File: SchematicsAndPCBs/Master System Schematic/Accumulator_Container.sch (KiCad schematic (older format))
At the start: 23 parts, among them J1 Shutdown/Precharge Connector, J2 TSAL Connector, J3 Main TS Connector, J4 IMD/TSMP Connector, K1 SPST-NO (Precharge), K2 SPST-NO (AIR), K3 SPST-NO (AIR), K4 SPST-NC (Discharge), K5 SPDT (Precharge Control), SW1 HVD, SW2 SMD, SW3 SMD, U1 TSAL_ISOLATION

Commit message: Updating Library References
Shifting references in the Master Schematic project to use the new NER library
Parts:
- U1: symbol TSV-rescue:TSAL_ISOLATION-FSAE-TSV-shematic-rescue -> NER:TSAL_ISOLATION
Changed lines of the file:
@@
 EESchema Schematic File Version 4
+LIBS:Master System Schematic-cache
 EELAYER 30 0
 EELAYER END
@@
 $EndDescr
 $Comp
-L TSV-rescue:TSAL_ISOLATION-FSAE-TSV-shematic-rescue U1
+L NER:TSAL_ISOLATION U1
 U 1 1 5E5145FA
 P 9900 5450
+AR Path="/5E5145FA" Ref="U1"  Part="1"
+AR Path="/5F45B05E/5E5145FA" Ref="U1"  Part="1"
 F 0 "U1" H 9925 5565 50  0000 C CNN
 F 1 "TSAL_ISOLATION" H 9900 5500 50  0000 C CNN

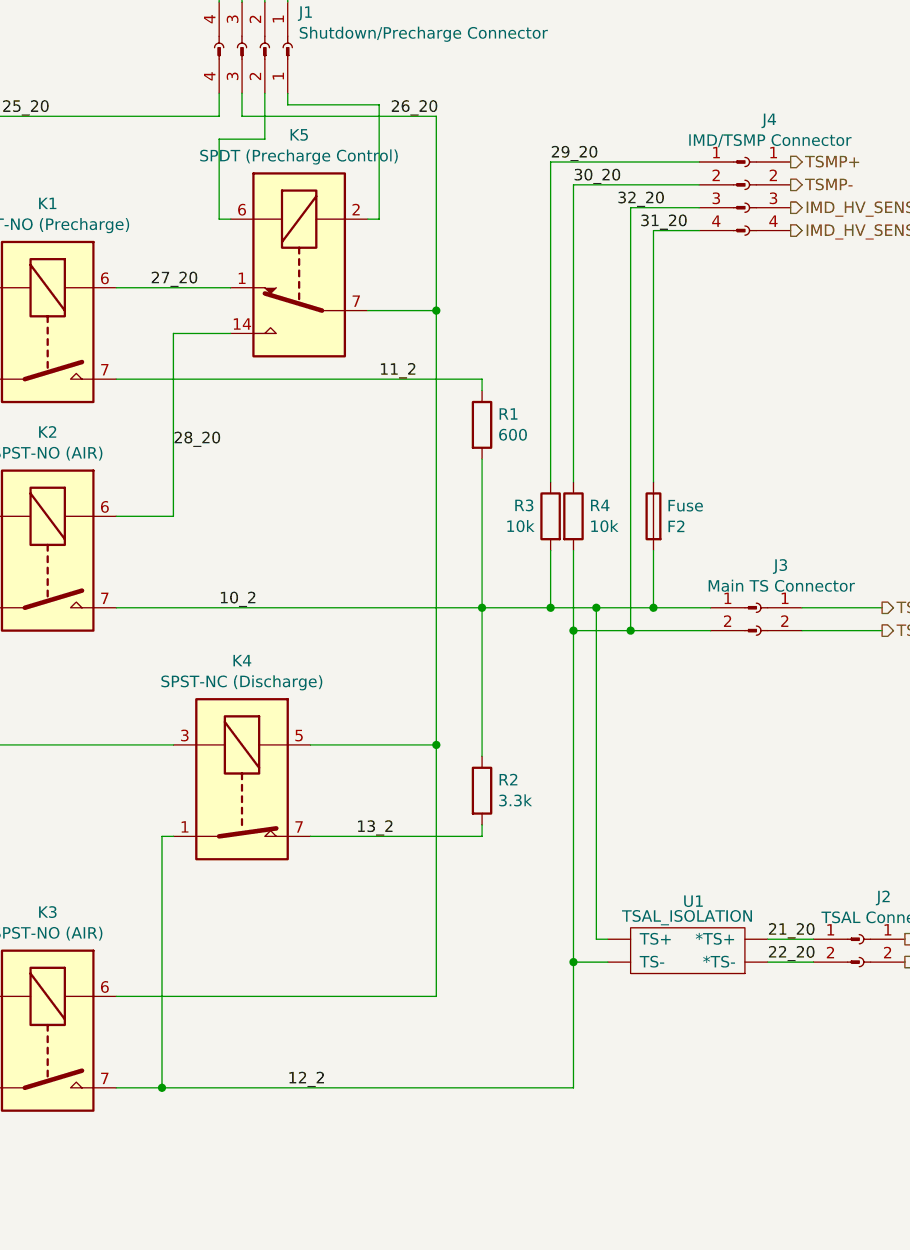
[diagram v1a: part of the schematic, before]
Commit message: Added new IMD fuse
Needed both sense lines to be fused. Added F3 to represent this
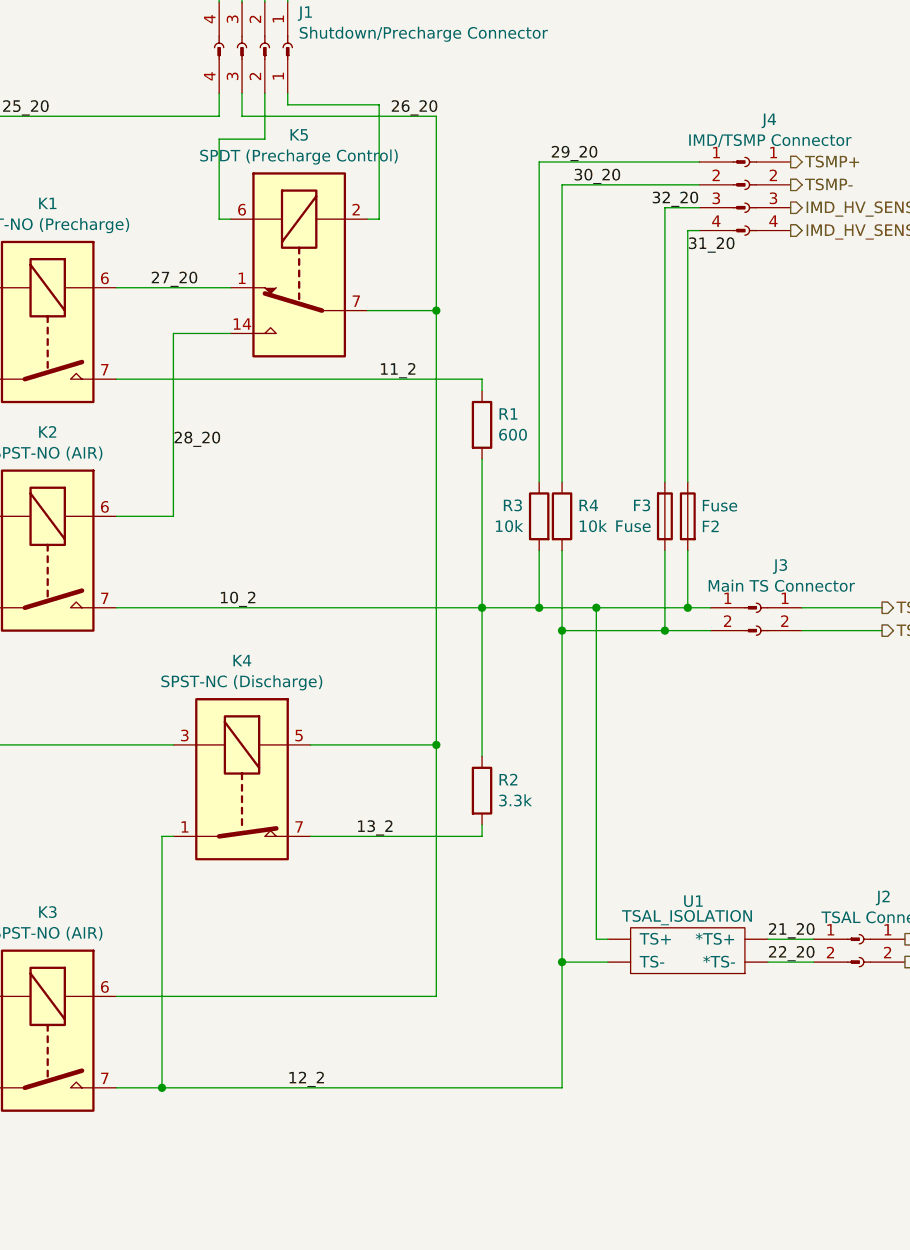
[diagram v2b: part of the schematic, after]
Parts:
- added F3: Fuse, symbol Device:Fuse
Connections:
- net 12_2: now also F3.1; no longer J?.3 (Pin_3)
- new net 32_20: F3.2, J?.3 (Pin_3)
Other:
- moved on the sheet: F2, R3, R4
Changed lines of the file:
@@
 L Device:R R3
 U 1 1 5F2AF3BD
-P 9300 3650
-F 0 "R3" H 9370 3696 50  0000 L CNN
-F 1 "10k" H 9370 3605 50  0000 L CNN
-F 2 "" V 9230 3650 50  0001 C CNN
-F 3 "~" H 9300 3650 50  0001 C CNN
-	1    9300 3650
+P 9250 3650
+F 0 "R3" H 9320 3696 50  0000 L CNN
+F 1 "10k" H 9320 3605 50  0000 L CNN
+F 2 "" V 9180 3650 50  0001 C CNN
+F 3 "~" H 9250 3650 50  0001 C CNN
+	1    9250 3650
 	-1   0    0    -1
 $EndComp
@@
 L Device:R R4
 U 1 1 5F39A796
-P 9400 3650
-F 0 "R4" H 9470 3696 50  0000 L CNN
-F 1 "10k" H 9470 3605 50  0000 L CNN
-F 2 "" V 9330 3650 50  0001 C CNN
-F 3 "~" H 9400 3650 50  0001 C CNN
-	1    9400 3650
+P 9350 3650
+F 0 "R4" H 9420 3696 50  0000 L CNN
+F 1 "10k" H 9420 3605 50  0000 L CNN
+F 2 "" V 9280 3650 50  0001 C CNN
+F 3 "~" H 9350 3650 50  0001 C CNN
+	1    9350 3650
 	1    0    0    -1
 $EndComp
@@
 L Device:Fuse F2
 U 1 1 5F14BDC4
-P 9750 3650
-F 0 "F2" H 9691 3604 50  0000 R CNN
-F 1 "Fuse" H 9691 3695 50  0000 R CNN
-F 2 "" V 9680 3650 50  0001 C CNN
-F 3 "~" H 9750 3650 50  0001 C CNN
-	1    9750 3650
+P 9900 3650
+F 0 "F2" H 9841 3604 50  0000 R CNN
+F 1 "Fuse" H 9841 3695 50  0000 R CNN
+F 2 "" V 9830 3650 50  0001 C CNN
+F 3 "~" H 9900 3650 50  0001 C CNN
+	1    9900 3650
 	-1   0    0    -1
 $EndComp
 Wire Wire Line
-	9750 3800 9750 4050
+	9900 3800 9900 4050
 Text Label 9300 2100 0    50   ~ 0
 29_20
 Text Label 9400 2200 0    50   ~ 0
 30_20
-Text Label 9900 2400 2    50   ~ 0
+Text Label 9900 2500 0    50   ~ 0
 31_20
-Text Label 9800 2300 2    50   ~ 0
+Text Label 9950 2300 2    50   ~ 0
 32_20
 Text Notes 7350 7500 0    50   ~ 0
@@
 $EndComp
 Wire Wire Line
-	9300 2100 9300 3500
-Wire Wire Line
-	9400 2200 9400 3500
-Wire Wire Line
-	9650 2300 9650 4150
-Wire Wire Line
-	9750 2400 9750 3500
-Wire Wire Line
-	9300 2100 9950 2100
-Wire Wire Line
-	9400 2200 9950 2200
-Wire Wire Line
-	9650 2300 9950 2300
-Wire Wire Line
-	9750 2400 9950 2400
-Connection ~ 9300 4050
-Wire Wire Line
-	9300 4050 9300 3800
-Wire Wire Line
-	9000 4050 9300 4050
-Wire Wire Line
-	9300 4050 9500 4050
-Wire Wire Line
-	9400 4150 9650 4150
-Wire Wire Line
-	9400 3800 9400 4150
-Connection ~ 9400 4150
-Connection ~ 9400 5600
-Wire Wire Line
-	9400 4150 9400 5600
+	9250 2100 9250 3500
+Wire Wire Line
+	9350 2200 9350 3500
+Wire Wire Line
+	9800 2300 9800 3500
+Wire Wire Line
+	9900 2400 9900 3500
+Wire Wire Line
+	9800 2300 9950 2300
+Wire Wire Line
+	9900 2400 9950 2400
+Wire Wire Line
+	9250 4050 9250 3800
+Wire Wire Line
+	9000 4050 9250 4050
 Wire Wire Line
 	10250 5500 10450 5500
@@
 Connection ~ 9500 4050
 Wire Wire Line
-	9500 4050 9750 4050
-Wire Wire Line
-	9400 5600 9550 5600
-Wire Wire Line
-	9400 5600 9400 6150
-Wire Wire Line
-	7600 6150 9400 6150
-Connection ~ 9750 4050
-Connection ~ 9650 4150
+	7600 6150 9350 6150
 Wire Wire Line
 	10750 4050 10400 4050
 Wire Wire Line
 	10400 4150 10750 4150
-Wire Wire Line
-	9750 4050 10000 4050
-Wire Wire Line
-	9650 4150 10000 4150
 $Sheet
 S 3200 4800 1550 2350
@@
 Wire Bus Line
 	550  7750 5500 7750
+$Comp
+L Device:Fuse F3
+U 1 1 5F6433FB
+P 9800 3650
+F 0 "F3" H 9741 3604 50  0000 R CNN
+F 1 "Fuse" H 9741 3695 50  0000 R CNN
+F 2 "" V 9730 3650 50  0001 C CNN
+F 3 "~" H 9800 3650 50  0001 C CNN
+	1    9800 3650
+	1    0    0    1
+$EndComp
+Wire Wire Line
+	9800 3800 9800 4150
+Connection ~ 9800 4150
+Wire Wire Line
+	9800 4150 10000 4150
+Connection ~ 9900 4050
+Wire Wire Line
+	9900 4050 10000 4050
+Wire Wire Line
+	9500 4050 9900 4050
+Connection ~ 9250 4050
+Wire Wire Line
+	9250 4050 9500 4050
+Wire Wire Line
+	9350 2200 9950 2200
+Wire Wire Line
+	9250 2100 9950 2100
+Wire Wire Line
+	9350 3800 9350 4150
+Wire Wire Line
+	9350 5600 9550 5600
+Connection ~ 9350 5600
+Wire Wire Line
+	9350 5600 9350 6150
+Wire Wire Line
+	9350 4150 9800 4150
 Wire Bus Line
 	3100 1100 3100 1350
@@
 Wire Bus Line
 	3100 4950 3100 6050
+Connection ~ 9350 4150
+Wire Wire Line
+	9350 4150 9350 5600
 $EndSCHEMATC

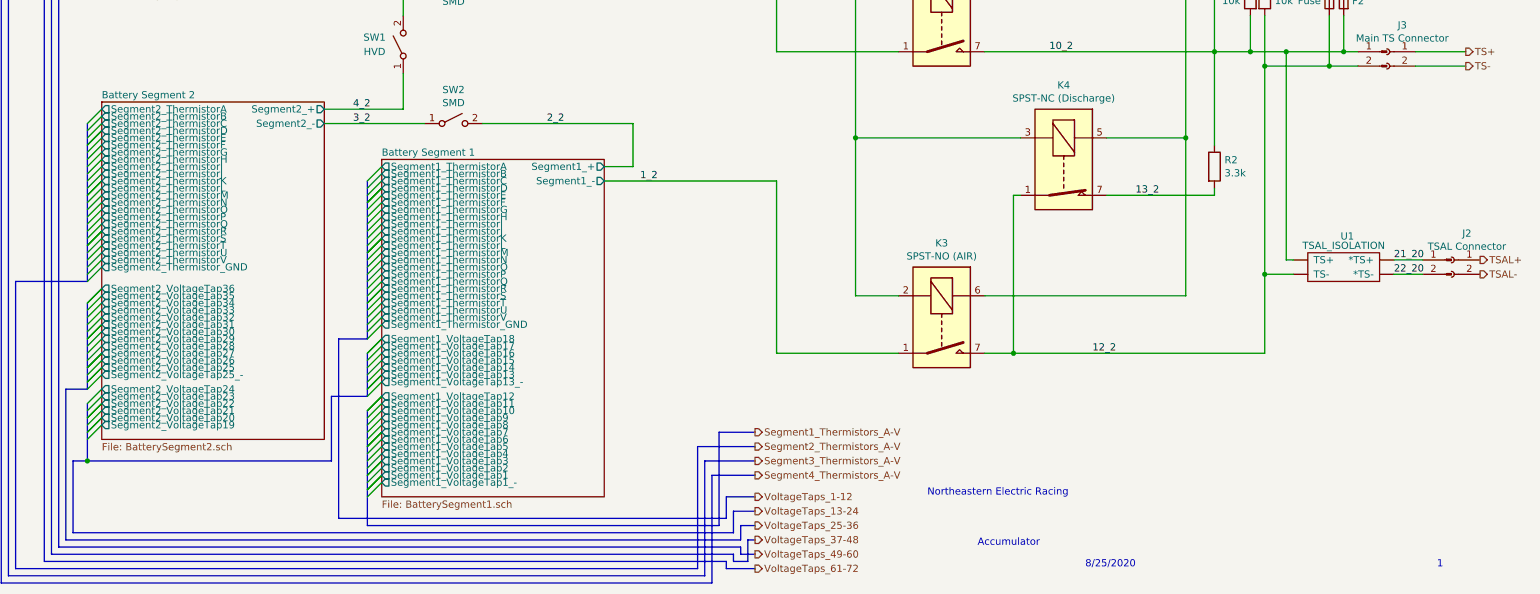
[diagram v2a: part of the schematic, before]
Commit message: Paper Size and Title Blocks
-Switched all paper sizes over to America units  (letter size A and tabloid size B) (so we can actually be cool and print them an stuff)
-Fixed title blocks to use sheet properties
-Started some changes to the accumulator segment schematic
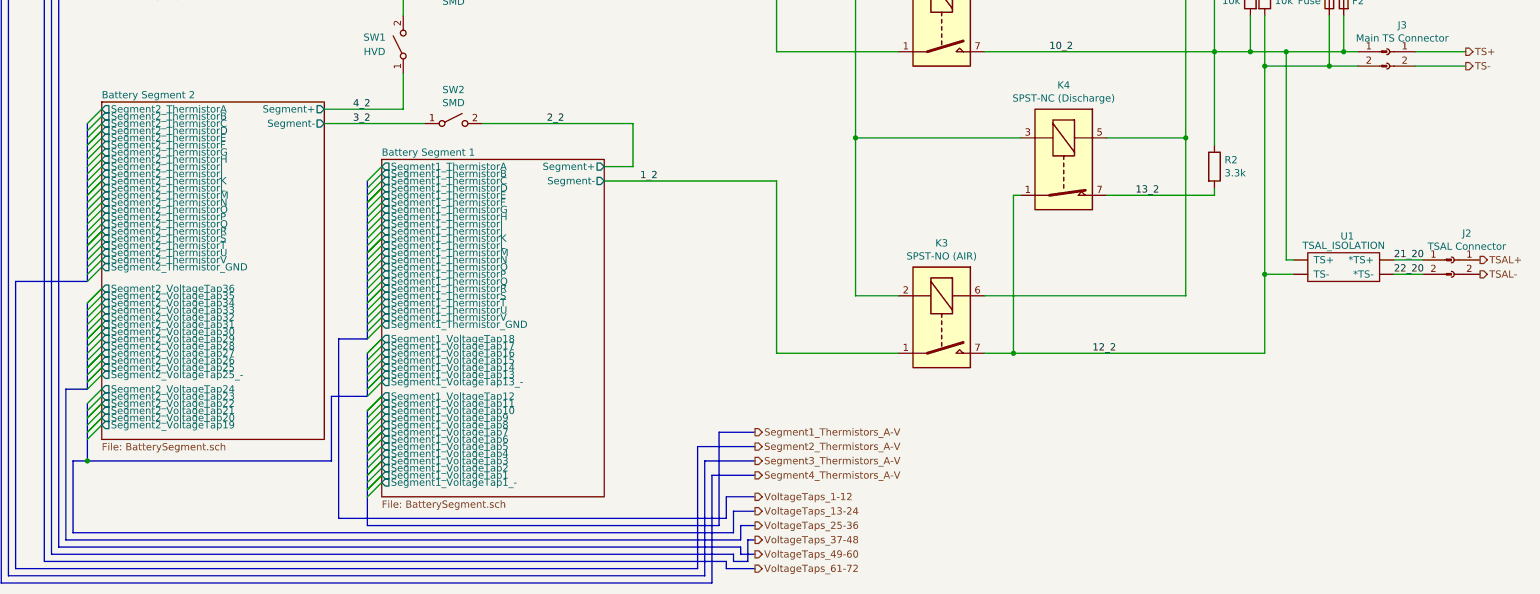
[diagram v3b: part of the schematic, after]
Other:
- note removed: "1"
- note removed: "8/25/2020"
- note removed: "Accumulator"
- note removed: "Northeastern Electric Racing"

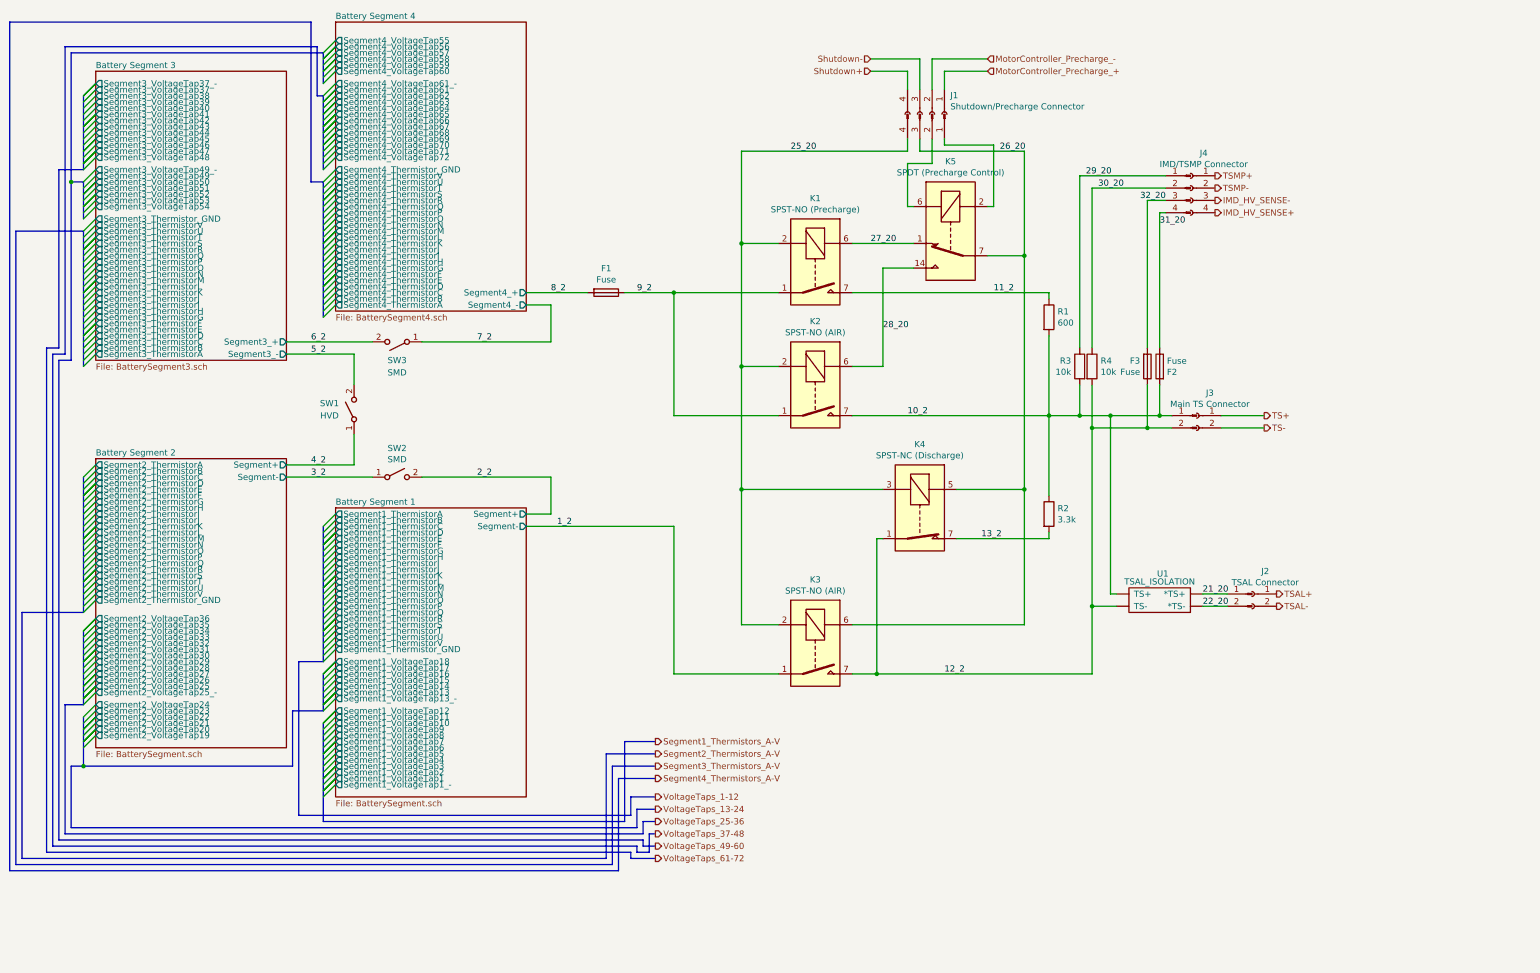
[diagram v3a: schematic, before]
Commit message: Therms and Volt Taps
Mostly fixed all thermistor and volt taps
Also created new sheet for BMS container and updated library part for OrionThermExpansionModule
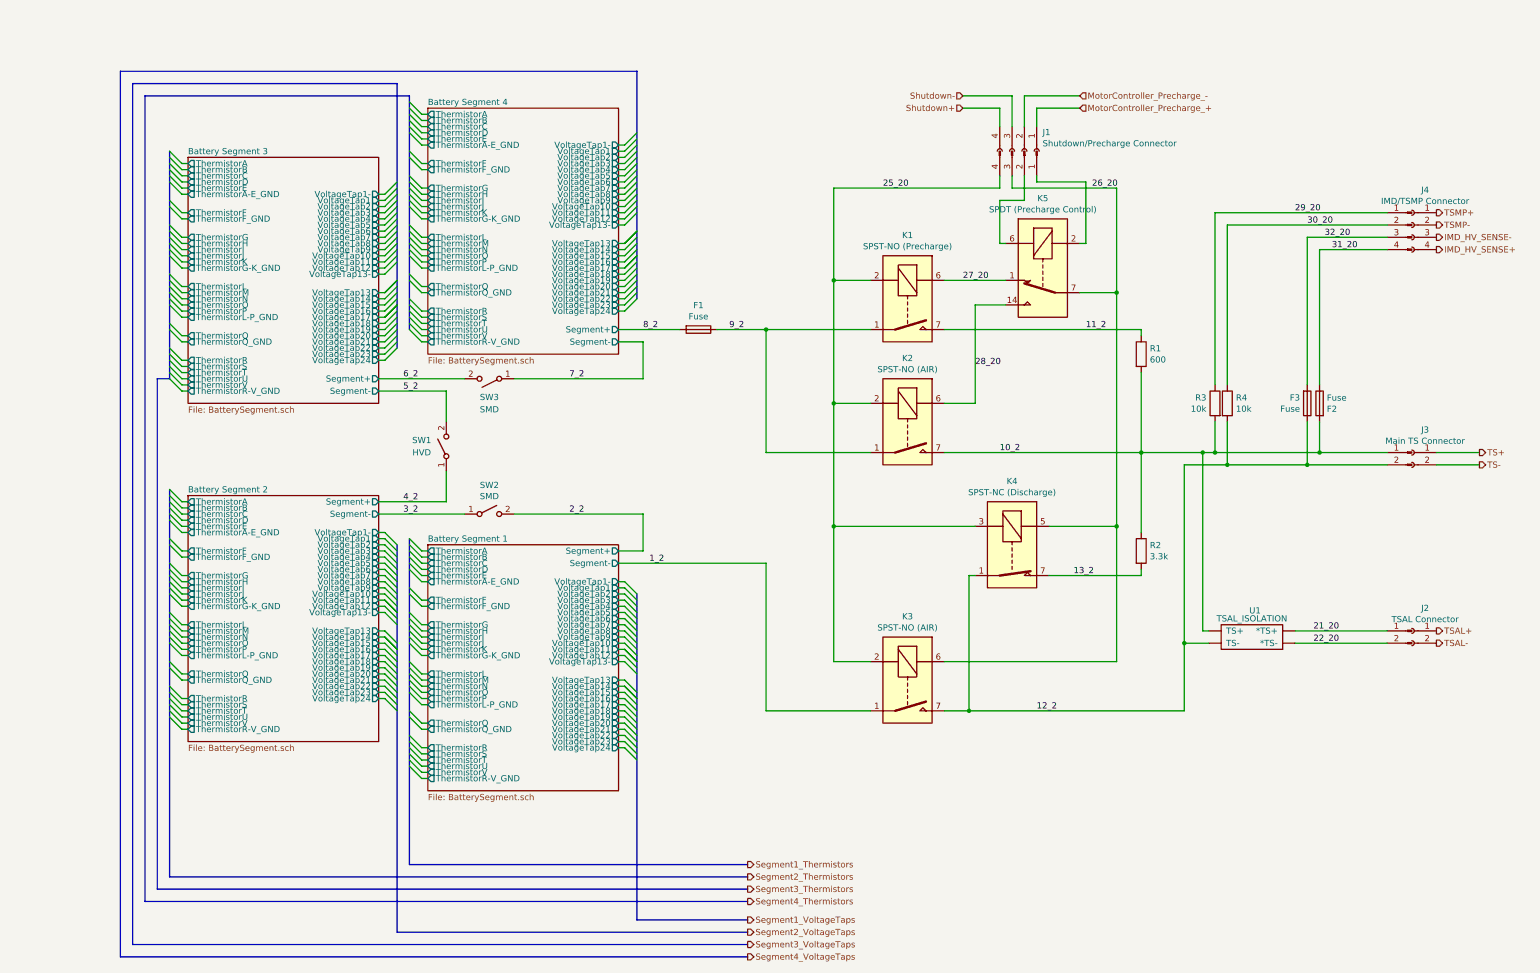
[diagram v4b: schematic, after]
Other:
- moved on the sheet: F1, F2, F3, J1, J2, J3, J4, K1, K2, K3, K4, K5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
